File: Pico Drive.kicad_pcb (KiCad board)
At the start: 2 copper layers, 100.3 x 102.2 mm, 23 parts, among them J1 Conn_01x06_Male, J2 Conn_01x08, J3 Conn_01x02_Male, J4 Conn_01x02_Male, SW1 Reset, U1 Pico, U2 74AXP1T45GWH, U3 74AHCT1G125, U4 OLED-I2C-Module-Aliexpress

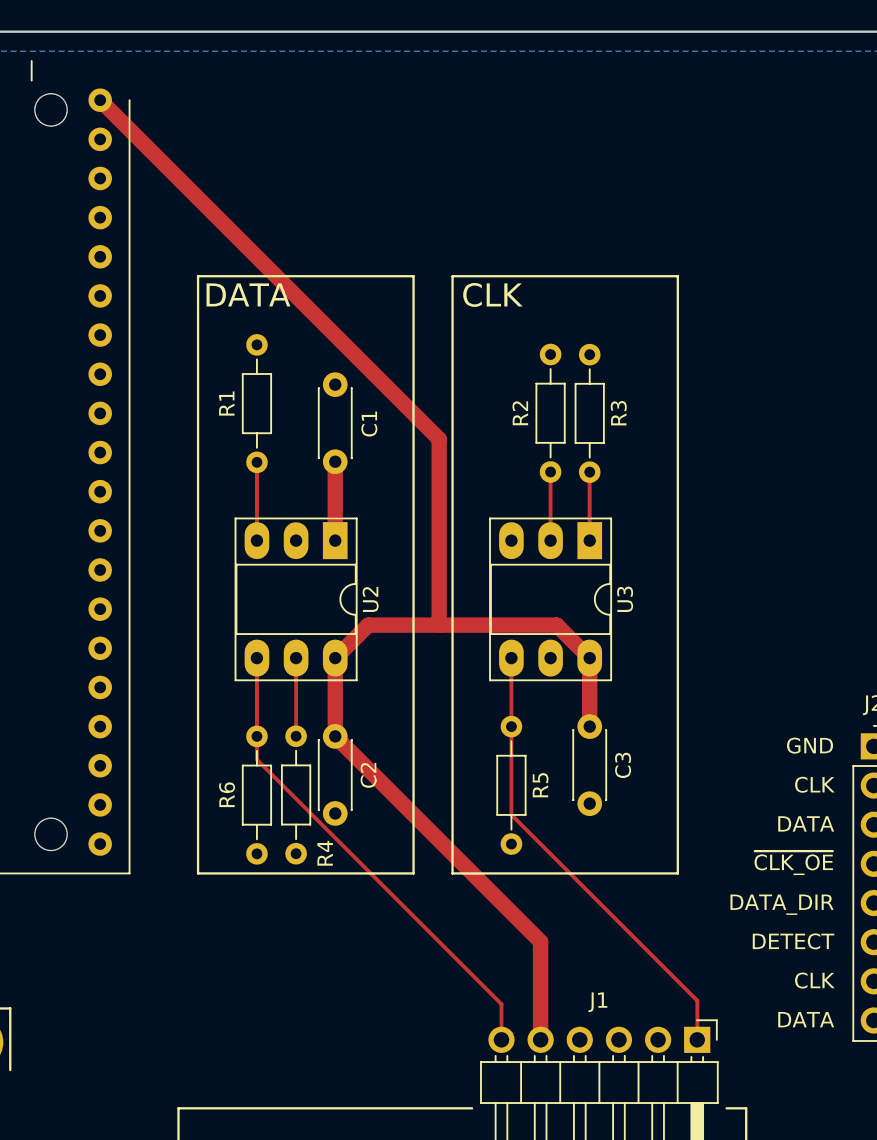
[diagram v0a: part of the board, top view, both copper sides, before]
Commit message: Rotated CLK and DATA on PCB
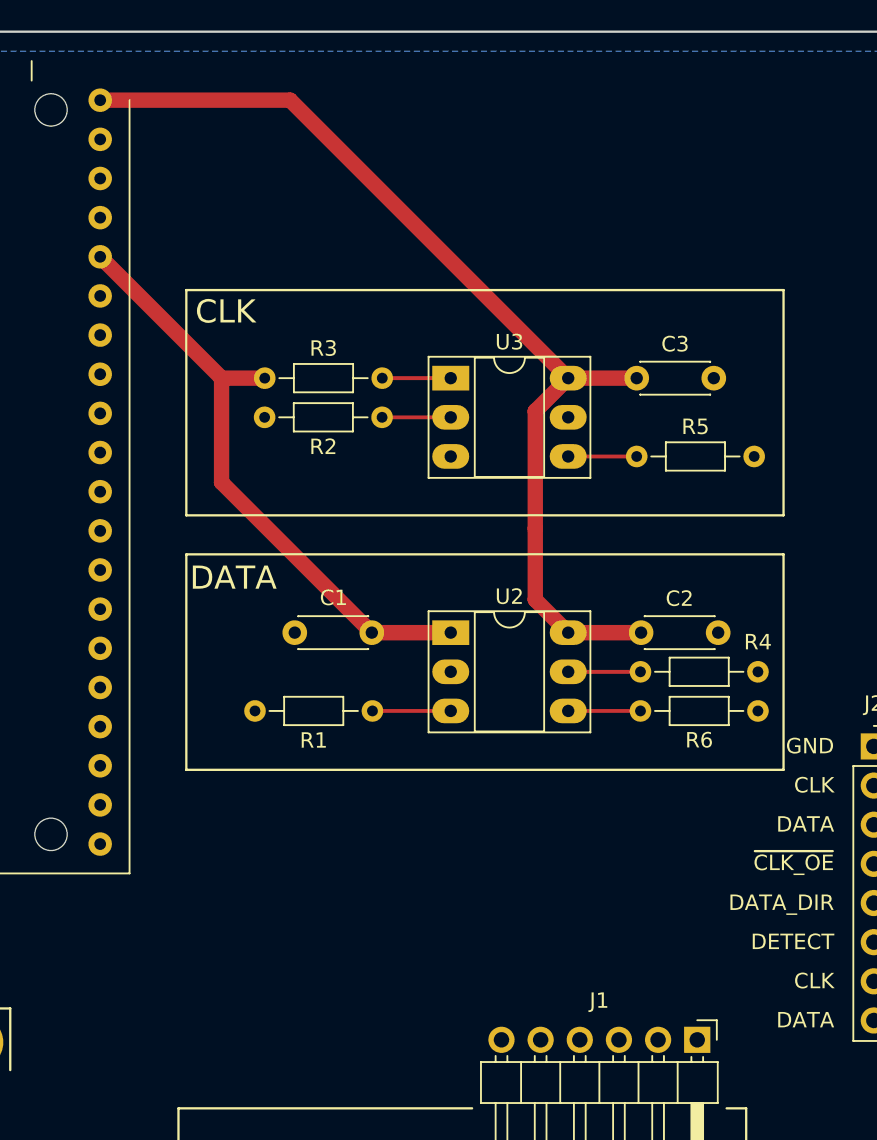
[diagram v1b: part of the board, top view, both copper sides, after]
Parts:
- moved R6 24.9 mm to (97.3, 59.3), turned to 0 degrees
- moved C3 22.8 mm to (97.0, 37.7), turned to 0 degrees
- moved R4 22.7 mm to (97.3, 56.8), turned to 0 degrees
- moved R3 21.1 mm to (72.9, 37.7), turned to 0 degrees
- moved C2 21.0 mm to (97.3, 54.2), turned to 0 degrees
- moved R5 19.3 mm to (97.0, 42.8), turned to 0 degrees
- moved R1 17.8 mm to (79.9, 59.3), turned to 180 degrees
- moved U3 13.9 mm to (85.0, 37.7), turned to 0 degrees
- moved R2 11.5 mm to (80.5, 40.3), turned to 180 degrees
- moved C1 11.3 mm to (79.9, 54.2), turned to 180 degrees
- moved U2 9.58 mm to (85.0, 54.2), turned to 0 degrees
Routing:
- net +3V3: track 5.12 -> 39.6 mm
- net +5V: track 96.2 -> 65.3 mm
- net /DATA_5V: track 31.3 -> 4.69 mm
- net /CLK_5V: track 29.8 -> 4.44 mm

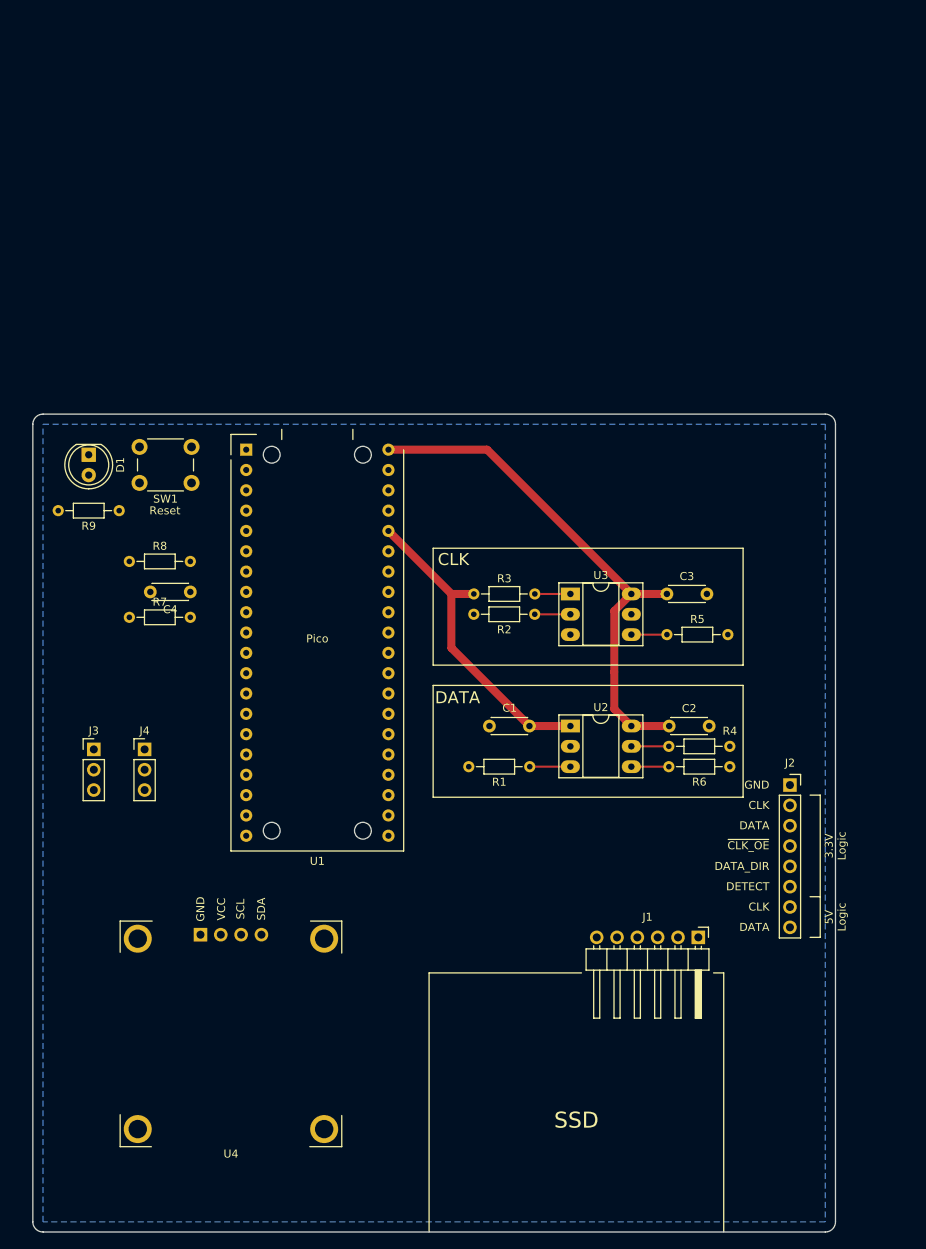
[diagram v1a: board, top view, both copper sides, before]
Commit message: Added space for Vpp circuitry
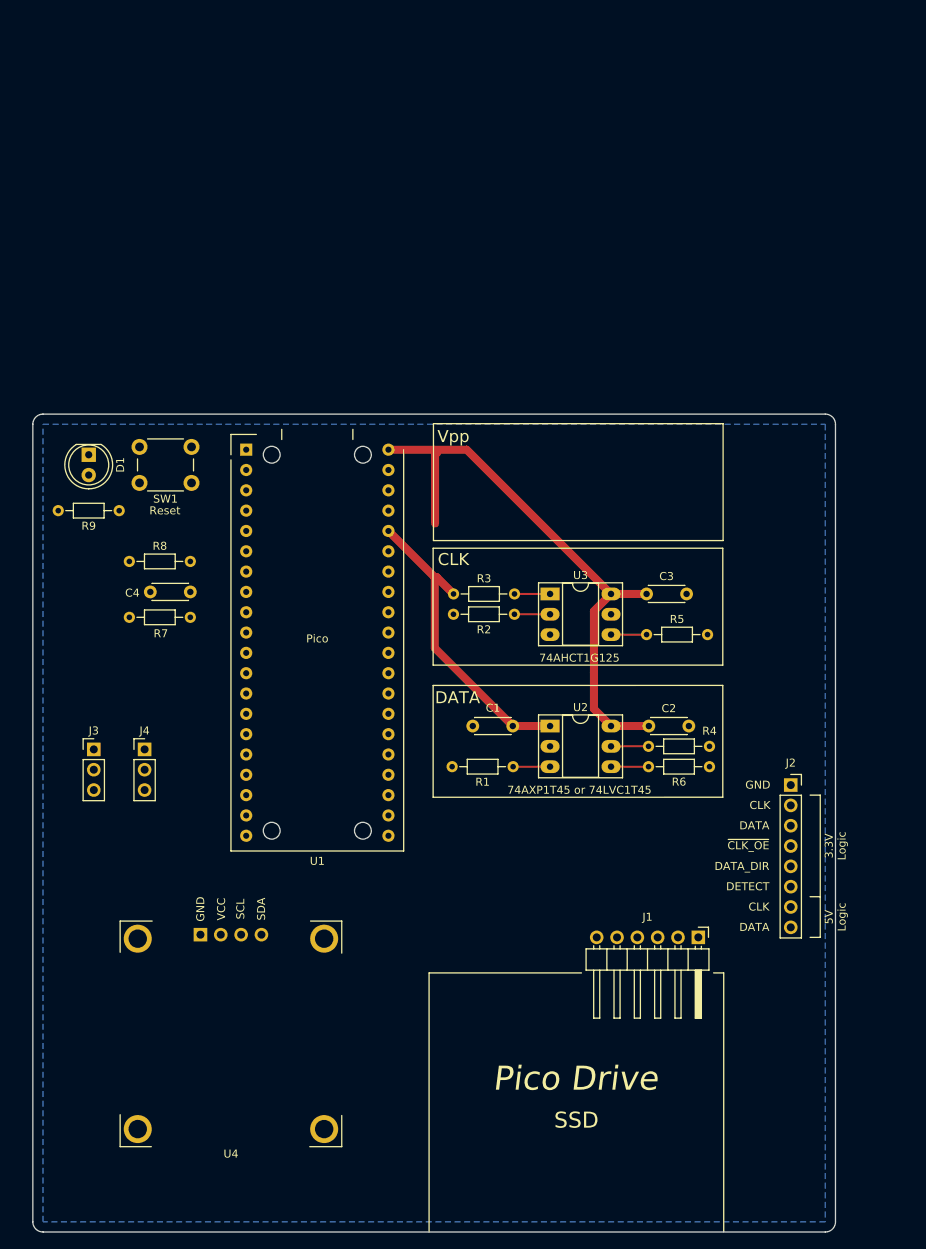
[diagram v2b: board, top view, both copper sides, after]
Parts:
- moved C2 2.54 mm to (94.8, 54.2)
- moved R2 2.54 mm to (78.0, 40.3)
- moved R3 2.54 mm to (70.4, 37.7)
- moved C3 2.54 mm to (94.5, 37.7)
- moved R4 2.54 mm to (94.7, 56.8)
- moved R5 2.54 mm to (94.5, 42.8)
- moved R6 2.54 mm to (94.7, 59.3)
- moved U2 2.54 mm to (82.4, 54.2)
- moved U3 2.54 mm to (82.4, 37.7)
- moved C1 2.08 mm to (77.8, 54.2)
- moved R1 2.08 mm to (77.8, 59.3)
- moved J2 0.10 mm to (112.5, 61.6)
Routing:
- net +5V: track 65.3 -> 71.9 mm
- net +3V3: track 39.6 -> 38.7 mm
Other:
- board text added: "74AHCT1G125"
- board text added: "74AXP1T45 or 74LVC1T45"
- board text added: "Pico Drive"
- board text added: "Vpp"

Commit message: Shifted bits around, ran power, added cutout
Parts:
- added H1: MountingHole, MountingHole:MountingHole_2.2mm_M2, F.Cu at (115.3, 18.0)
- added H2: MountingHole, MountingHole:MountingHole_2.2mm_M2, F.Cu at (20.6, 18.0)
- added H3: MountingHole, MountingHole:MountingHole_2.2mm_M2, F.Cu at (20.8, 114.6)
- added H4: MountingHole, MountingHole:MountingHole_2.2mm_M2, F.Cu at (115.1, 114.6)
- added REF**: TestPoint_Pad_2.0x2.0mm, TestPoint:TestPoint_Pad_2.0x2.0mm, F.Cu at (100.8, 30.5)
- added REF**: TestPoint_Pad_2.0x2.0mm, TestPoint:TestPoint_Pad_2.0x2.0mm, F.Cu at (100.8, 23.1)
- added REF**: TestPoint_Pad_2.0x2.0mm, TestPoint:TestPoint_Pad_2.0x2.0mm, F.Cu at (67.8, 23.1)
- added REF**: TestPoint_Pad_2.0x2.0mm, TestPoint:TestPoint_Pad_2.0x2.0mm, F.Cu at (67.8, 30.5)
- SW1: footprint Button_Switch_THT:SW_PUSH_6mm -> Button_Switch_THT:SW_PUSH_6mm_H4.3mm
- U2, U3: footprint Package_DIP:DIP-6_W7.62mm_Socket_LongPads -> Package_DIP:DIP-6_W7.62mm_Socket
- moved J3 11.9 mm to (27.4, 45.5)
- moved R7 11.2 mm to (40.6, 37.8), turned to 180 degrees
- moved R9 6.76 mm to (22.6, 30.5), turned to 0 degrees
- moved J2 4.84 mm to (110.6, 57.2)
- moved R8 4.49 mm to (33.0, 30.5)
- moved J4 4.33 mm to (27.4, 56.9)
- moved C4 4.23 mm to (40.6, 34.7)
- moved D1 3.89 mm to (26.4, 23.8), turned to 90 degrees
- moved C3 3.28 mm to (92.7, 40.5)
- moved R5 3.28 mm to (92.7, 45.5)
- moved U3 3.28 mm to (80.6, 40.5)
- moved R2 3.28 mm to (76.2, 43.0)
- moved R3 3.28 mm to (68.6, 40.5)
- moved SW1 2.67 mm to (40.1, 24.9)
- moved R1 2.60 mm to (76.0, 61.2)
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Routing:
- net +3V3: track 38.7 -> 143.7 mm
- net /~{RUN}: track 0.00 -> 58.9 mm
- net Net-(R7-Pad2): track 0.00 -> 18.4 mm
- net +5V: track 71.9 -> 57.0 mm
- net Net-(D1-Pad2): track 0.00 -> 10.8 mm
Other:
- outline, holes or cut-outs redrawn
- board text added: "Power"

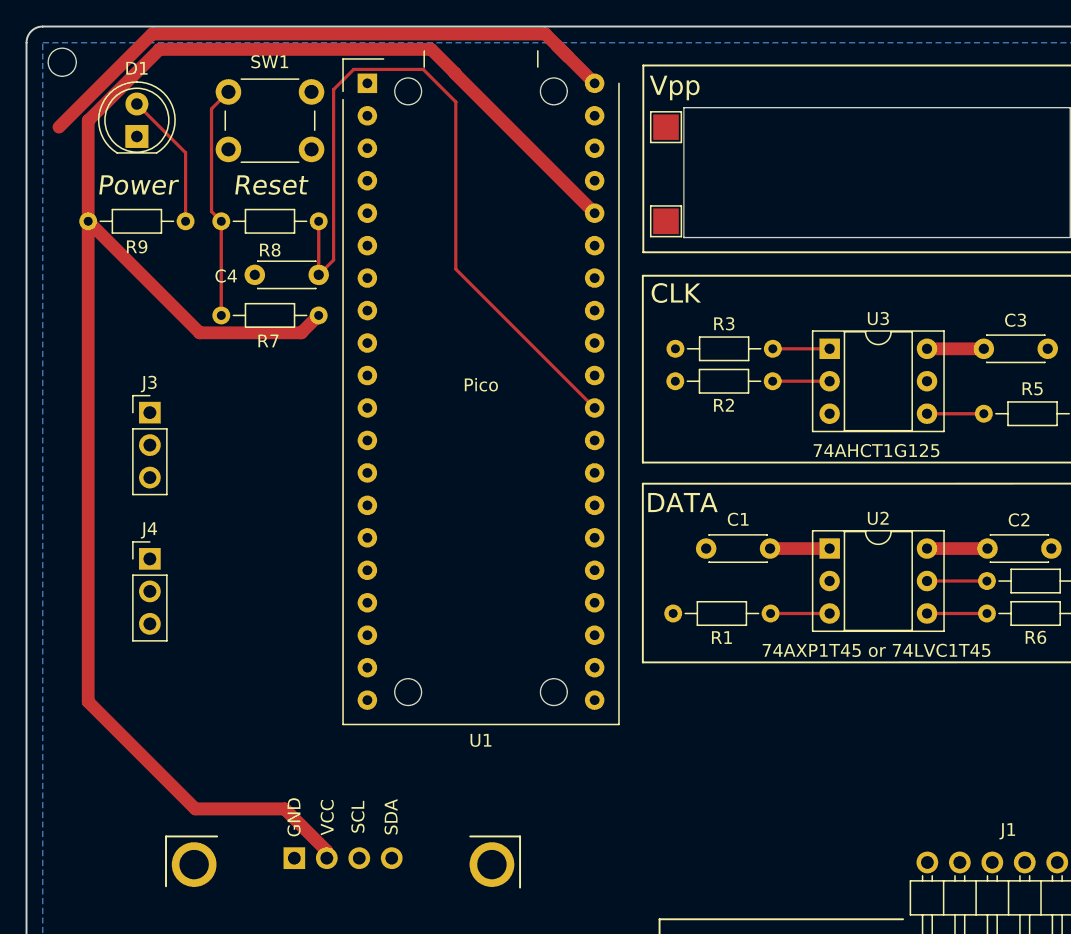
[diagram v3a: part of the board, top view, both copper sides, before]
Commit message: Cleared out old traces ready for overhaul
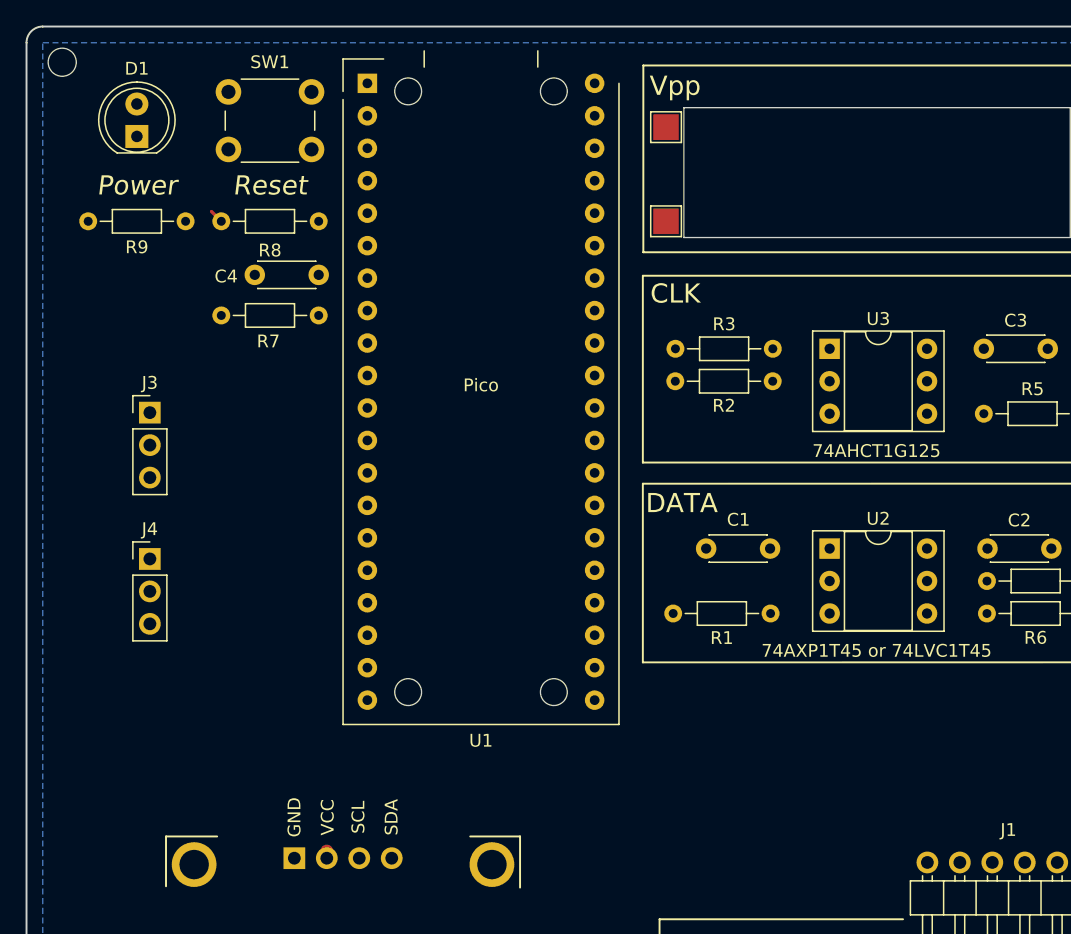
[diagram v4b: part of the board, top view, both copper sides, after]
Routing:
- net +3V3: track 143.7 -> 0.56 mm
- net /~{RUN}: track 58.9 -> 0.00 mm
- net +5V: track 57.0 -> 0.00 mm
- net Net-(R7-Pad2): track 18.4 -> 1.08 mm
- net Net-(D1-Pad2): track 10.8 -> 0.00 mm
- net /DATA_DIR: track 4.69 -> 0.00 mm
- net /DATA_5V: track 4.69 -> 0.00 mm
- net /DATA_3V3: track 4.62 -> 0.00 mm
- net /CLK_3V3: track 4.45 -> 0.00 mm
- net /~{CLK_OE}: track 4.45 -> 0.00 mm
- net /CLK_5V: track 4.44 -> 0.00 mm
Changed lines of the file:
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@@
   )
   (segment (start 41.275 79.75) (end 41.275 80.31) (width 1) (layer "F.Cu") (net 28))
-  (segment (start 31.334179 39.208179) (end 22.606 30.48) (width 1) (layer "F.Cu") (net 28))
-  (segment (start 51.308 18.891829) (end 51.308 18.923) (width 1) (layer "F.Cu") (net 28))
-  (segment (start 22.606 30.48) (end 22.606 68.072) (width 1) (layer "F.Cu") (net 28))
-  (segment (start 51.308 18.891829) (end 49.440001 17.02383) (width 1) (layer "F.Cu") (net 28))
-  (segment (start 51.308 18.923) (end 62.23 29.845) (width 1) (layer "F.Cu") (net 28))
-  (segment (start 49.440001 17.02383) (end 28.18817 17.02383) (width 1) (layer "F.Cu") (net 28))
-  (segment (start 30.988 76.454) (end 37.979 76.454) (width 1) (layer "F.Cu") (net 28))
-  (segment (start 22.606 22.606) (end 22.606 30.48) (width 1) (layer "F.Cu") (net 28))
-  (segment (start 39.277821 39.208179) (end 31.334179 39.208179) (width 1) (layer "F.Cu") (net 28))
-  (segment (start 22.606 68.072) (end 30.988 76.454) (width 1) (layer "F.Cu") (net 28))
-  (segment (start 28.18817 17.02383) (end 22.606 22.606) (width 1) (layer "F.Cu") (net 28))
-  (segment (start 40.64 37.846) (end 39.277821 39.208179) (width 1) (layer "F.Cu") (net 28))
-  (segment (start 37.979 76.454) (end 41.275 79.75) (width 1) (layer "F.Cu") (net 28))
-  (segment (start 75.956 56.0855) (end 80.6165 56.0855) (width 1) (layer "F.Cu") (net 28))
-  (segment (start 88.2365 56.0855) (end 92.9655 56.0855) (width 1) (layer "F.Cu") (net 29))
-  (segment (start 60.1345 17.5895) (end 59.309 16.764) (width 1) (layer "F.Cu") (net 29))
-  (segment (start 62.23 19.685) (end 60.1345 17.5895) (width 1) (layer "F.Cu") (net 29))
-  (segment (start 59.309 16.764) (end 59.182 16.764) (width 0.25) (layer "F.Cu") (net 29))
-  (segment (start 88.2365 40.4545) (end 92.6815 40.4545) (width 1) (layer "F.Cu") (net 29))
-  (segment (start 58.36883 15.82383) (end 27.61017 15.82383) (width 1) (layer "F.Cu") (net 29))
-  (segment (start 60.1345 17.5895) (end 58.36883 15.82383) (width 1) (layer "F.Cu") (net 29))
-  (segment (start 27.61017 15.82383) (end 20.32 23.114) (width 1) (layer "F.Cu") (net 29))
-  (segment (start 76.1715 40.4545) (end 80.6165 40.4545) (width 0.25) (layer "F.Cu") (net 30))
-  (segment (start 51.3715 34.2265) (end 51.3715 21.1455) (width 0.25) (layer "F.Cu") (net 31))
-  (segment (start 40.64 30.48) (end 40.64 34.671) (width 0.25) (layer "F.Cu") (net 31))
-  (segment (start 43.378 18.598) (end 41.807865 20.168135) (width 0.25) (layer "F.Cu") (net 31))
-  (segment (start 62.23 45.085) (end 51.3715 34.2265) (width 0.25) (layer "F.Cu") (net 31))
-  (segment (start 51.3715 21.1455) (end 48.824 18.598) (width 0.25) (layer "F.Cu") (net 31))
-  (segment (start 41.807865 20.168135) (end 41.807865 33.503135) (width 0.25) (layer "F.Cu") (net 31))
-  (segment (start 41.807865 33.503135) (end 40.64 34.671) (width 0.25) (layer "F.Cu") (net 31))
-  (segment (start 48.824 18.598) (end 43.378 18.598) (width 0.25) (layer "F.Cu") (net 31))
-  (segment (start 75.996 61.1655) (end 80.6165 61.1655) (width 0.25) (layer "F.Cu") (net 32))
-  (segment (start 76.1615 42.9945) (end 80.6165 42.9945) (width 0.25) (layer "F.Cu") (net 33))
-  (segment (start 88.2365 58.6255) (end 92.9255 58.6255) (width 0.25) (layer "F.Cu") (net 34))
-  (segment (start 88.2365 45.5345) (end 92.6815 45.5345) (width 0.25) (layer "F.Cu") (net 35))
-  (segment (start 88.2365 61.1655) (end 92.9255 61.1655) (width 0.25) (layer "F.Cu") (net 36))
   (segment (start 32.255 29.715) (end 33.02 30.48) (width 0.25) (layer "F.Cu") (net 37))
-  (segment (start 33.58 20.356) (end 32.255 21.681) (width 0.25) (layer "F.Cu") (net 37))
-  (segment (start 33.02 30.48) (end 33.02 37.846) (width 0.25) (layer "F.Cu") (net 37))
-  (segment (start 32.255 21.681) (end 32.255 29.715) (width 0.25) (layer "F.Cu") (net 37))
-  (segment (start 26.416 21.302) (end 30.226 25.112) (width 0.25) (layer "F.Cu") (net 41))
-  (segment (start 30.226 25.112) (end 30.226 30.48) (width 0.25) (layer "F.Cu") (net 41))
   (zone (net 1) (net_name "GND") (layer "B.Cu") (hatch edge 0.508)
     (connect_pads (clearance 0.508))
